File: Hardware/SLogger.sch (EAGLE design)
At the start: 16 parts, among them U2 DSPIC33FJ802GP-28, U7 USD-SOCKETNEW

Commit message: Finished 1.0 version of the new SLogger hardware.
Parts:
- added JP1: M03PTH, ASL:M03PTH
- added U4: MCP2551, SparkFun:MCP2551
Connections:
- new net CAN_HI: JP1.3, U4.CANH
- new net CAN_LO: JP1.2, U4.CANL
- new net CAN_RX: U2.RB14, U4.RXD
- new net CAN_TX: U2.RB3, U4.TXD
- new net VCC5V0: U4.VDD
- net GND: now also JP1.1, U4.RS, U4.VSS

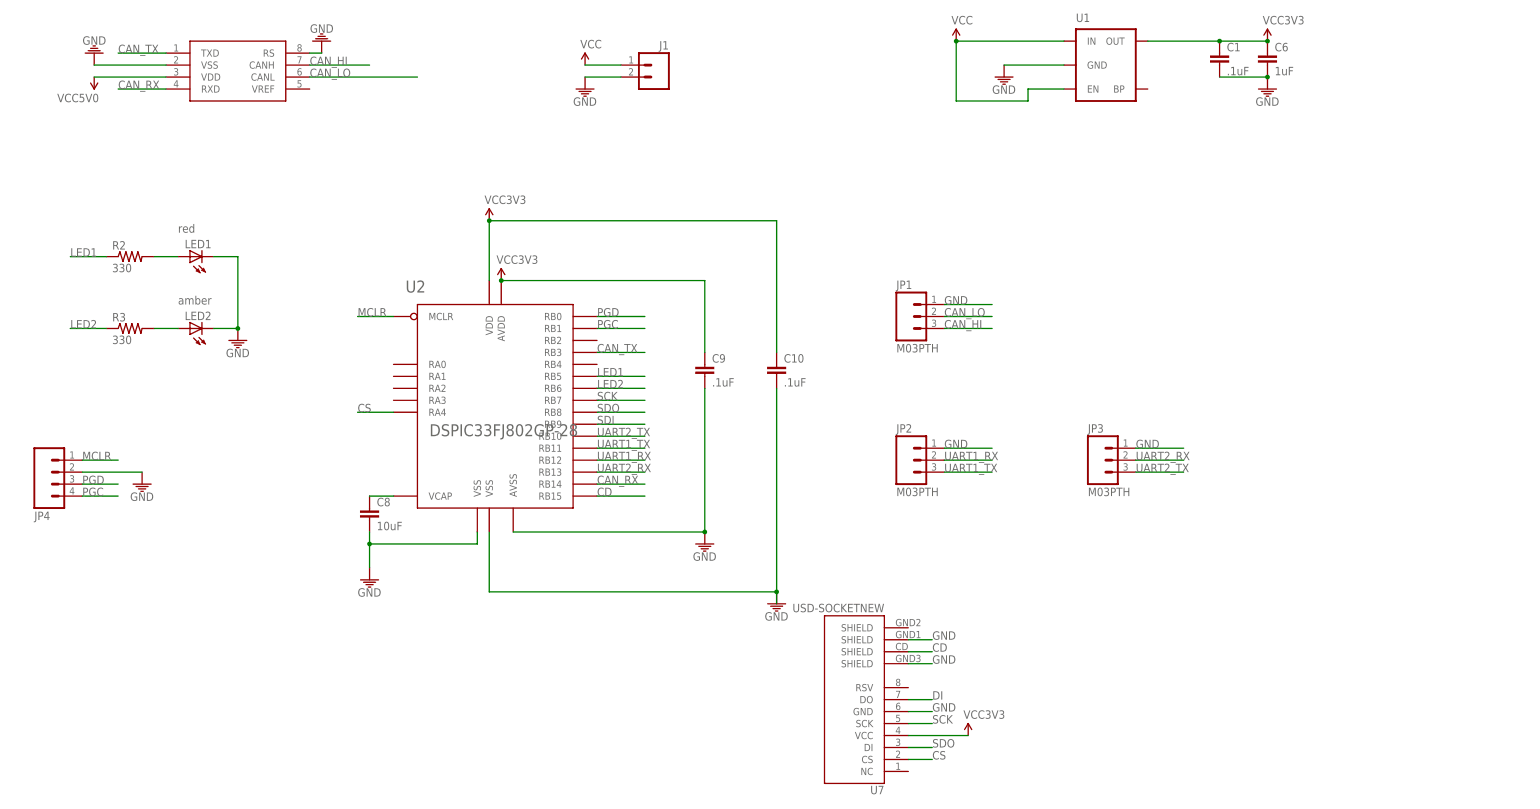
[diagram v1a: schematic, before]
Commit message: Added marcellos changes and documented.
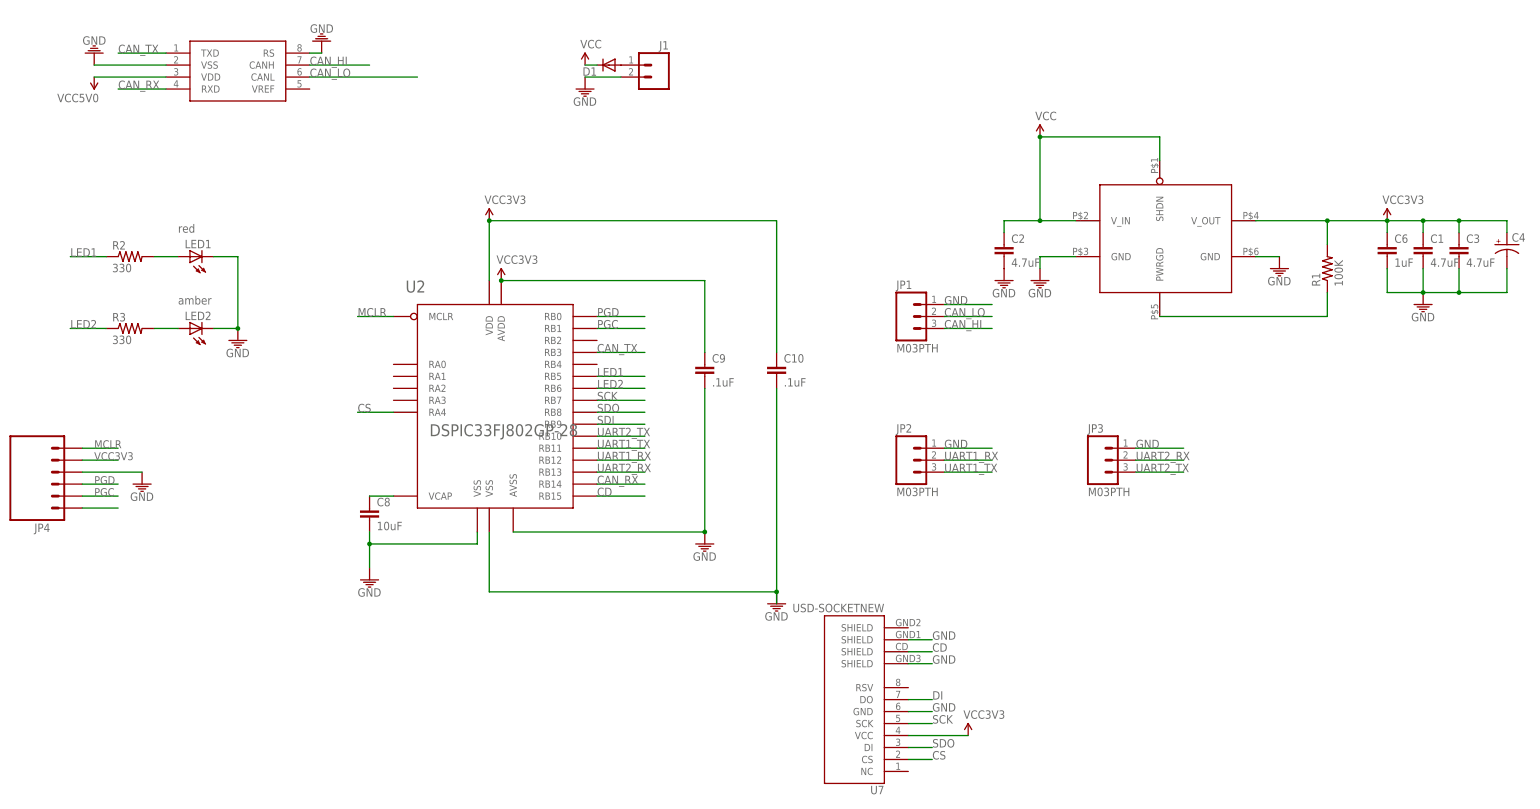
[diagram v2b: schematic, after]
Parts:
- removed U1: (no value), SparkFun-PowerIC:MIC52053.3V
- added C2, C3: 4.7uF, ASL:CAP0805
- added C4: (no value), ASL:CAP_POLPTH1
- added D1: (no value), ASL:DIODESOD
- added R1: 100K, CMPE118lib:RESISTOR0805-RES
- added U$2: MCP1826, ASL:MCP1826
- C1: value .1uF -> 4.7uF
- JP4: device SparkFun-Connectors:M04PTH -> ASL:M06LOCK
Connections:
- new net GND@3: U$2.GND@3
- new net GND@6: U$2.GND@6
- new net N$11: JP4.1
- new net N$2: D1.A, J1.2
- new net N$4: R1.1, U$2.PWRGD
- net GND: now also C2.2, C3.2, C4.-, JP4.4; no longer JP4.2, U1.GND
- net MCLR: now also JP4.6; no longer JP4.1
- net PGC: now also JP4.2; no longer JP4.4
- net VCC: now also C2.1, D1.C, U$2.SHDN, U$2.V_IN; no longer J1.2, U1.EN, U1.IN
- net VCC3V3: now also C3.1, C4.+, JP4.5, R1.2, U$2.V_OUT; no longer U1.OUT
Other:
- moved on the sheet: C1, C6, JP4
